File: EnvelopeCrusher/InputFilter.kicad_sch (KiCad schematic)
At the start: 6 parts, among them U1 TL072

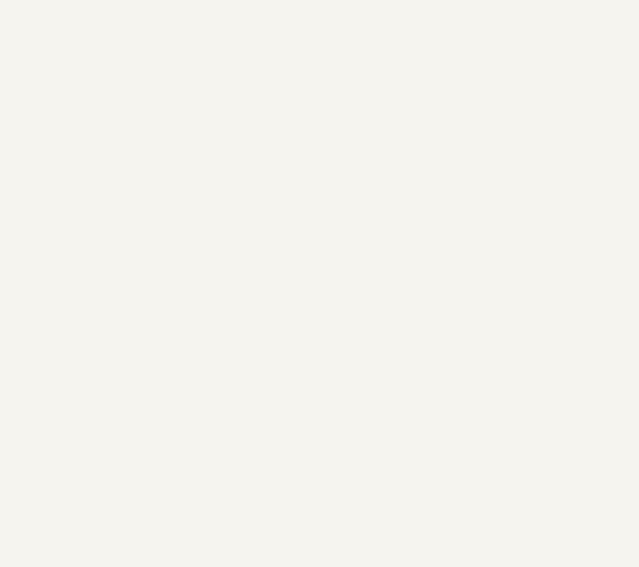
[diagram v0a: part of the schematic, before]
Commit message: updated signal path
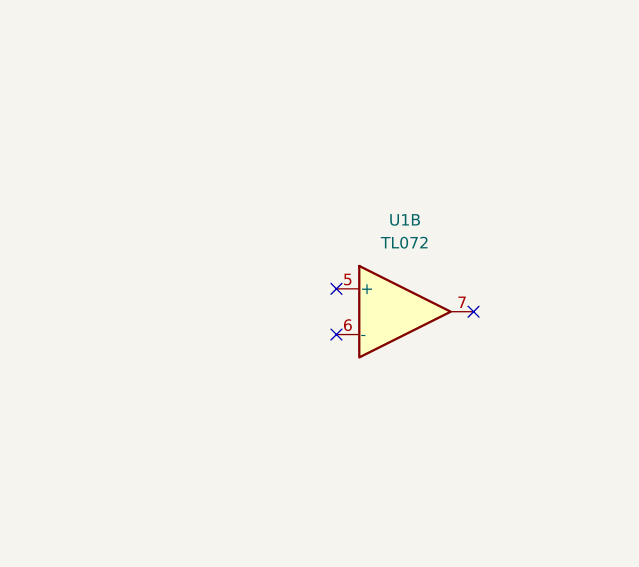
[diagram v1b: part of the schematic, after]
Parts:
- added unit 2 of U1
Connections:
- no-connect marks 0 -> 3
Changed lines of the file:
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@@
   (junction (at 130.81 135.89) (diameter 0) (color 0 0 0 0)
   )
+  (no_connect (at 222.25 139.7))
+  (no_connect (at 207.01 137.16))
+  (no_connect (at 207.01 142.24))
   (wire (pts (xy 130.81 135.89) (xy 143.51 135.89))
     (stroke (width 0) (type default) (color 0 0 0 0))
@@
     (pin "1")
   )
+  (symbol (lib_id "Amplifier_Operational:TL072") (at 214.63 139.7 0) (unit 2)
+    (in_bom yes) (on_board yes) (fields_autoplaced)
+    (property "Reference" "U1" (id 0) (at 214.63 129.54 0))
+    (property "Value" "TL072" (id 1) (at 214.63 132.08 0))
+    (property "Footprint" "" (id 2) (at 214.63 139.7 0)
+      (effects (font (size 1.27 1.27)) hide)
+    )
+    (property "Datasheet" "http://www.ti.com/lit/ds/symlink/tl071.pdf" (id 3) (at 214.63 139.7 0)
+      (effects (font (size 1.27 1.27)) hide)
+    )
+    (pin "1")
+    (pin "2")
+    (pin "3")
+    (pin "5")
+    (pin "6")
+    (pin "7")
+    (pin "4")
+    (pin "8")
+  )
   (symbol (lib_id "power:+5V") (at 67.31 130.1679 0) (unit 1)
